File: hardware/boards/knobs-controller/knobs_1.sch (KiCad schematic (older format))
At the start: 28 parts, among them J1 ZX62-AB-5PA(31), J4 JST---S4B-PH-SM4-TB(LF)(SN)_J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, J8 2X3_SMD_MALE, U3 MK1_ZERO_ATSAMD21G18A-48, Y1 32.768KHz

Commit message: redo migrate from eagle
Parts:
- C11, C4, C6, C9: footprint KnobsController_v1.1:RESISTOR-NICK_C0805 -> knobs:RESISTOR-NICK_C0805; symbol KnobsController_v1.1-eagle-import:RESISTOR-NICK_C-EUC0805 -> knobs-eagle-import:RESISTOR-NICK_C-EUC0805
- C5: footprint KnobsController_v1.1:RESISTOR-NICK_C1206 -> knobs:RESISTOR-NICK_C1206; symbol KnobsController_v1.1-eagle-import:RESISTOR-NICK_C-EUC1206 -> knobs-eagle-import:RESISTOR-NICK_C-EUC1206
- C7: footprint KnobsController_v1.1:C0805 -> knobs:C0805; symbol KnobsController_v1.1-eagle-import:C-EUC0805 -> knobs-eagle-import:C-EUC0805
- D1: footprint KnobsController_v1.1:MK1_ZERO_SOT190P230X110-4N -> knobs:MK1_ZERO_SOT190P230X110-4N; symbol KnobsController_v1.1-eagle-import:MK1_ZERO_PRTR5V0U2X,215 -> knobs-eagle-import:MK1_ZERO_PRTR5V0U2X,215
- D2: footprint KnobsController_v1.1:LED_RADIAL_3MM -> knobs:LED_RADIAL_3MM; symbol KnobsController_v1.1-eagle-import:LED_LTL-1CHG -> knobs-eagle-import:LED_LTL-1CHG
- D3: footprint KnobsController_v1.1:MK1_ZERO_SODFL1008X40N-882D -> knobs:MK1_ZERO_SODFL1008X40N-882D; symbol KnobsController_v1.1-eagle-import:MK1_ZERO_PMEG2005EL -> knobs-eagle-import:MK1_ZERO_PMEG2005EL
- F2: footprint KnobsController_v1.1:MK1_ZERO_0603-F1608X100N -> knobs:MK1_ZERO_0603-F1608X100N; symbol KnobsController_v1.1-eagle-import:MK1_ZERO_MF-FSMF050X-2 -> knobs-eagle-import:MK1_ZERO_MF-FSMF050X-2
- J1: footprint KnobsController_v1.1:MK1_ZERO_USBMICRO-ZX62-AB-5PA -> knobs:MK1_ZERO_USBMICRO-ZX62-AB-5PA; symbol KnobsController_v1.1-eagle-import:MK1_ZERO_ZX62AB-5PA(11) -> knobs-eagle-import:MK1_ZERO_ZX62AB-5PA(11)
- J4: footprint KnobsController_v1.1:JST---S4B-PH-SM4-TB(LF)(SN)_JST_S4B-PH-SM4-TB_LF_SN_0 -> knobs:JST---S4B-PH-SM4-TB(LF)(SN)_JST_S4B-PH-SM4-TB_LF_SN_0; symbol KnobsController_v1.1-eagle-import:JST---S4B-PH-SM4-TB(LF)(SN)_JST_S4B-PH-SM4-TB_LF_SNJST_S4B-PH-SM4-TB_LF_SN_0_0 -> knobs-eagle-import:JST---S4B-PH-SM4-TB(LF)(SN)_JST_S4B-PH-SM4-TB_LF_SNJST_S4B-PH-SM4-TB_LF_SN_0_0
- J8: footprint KnobsController_v1.1:2X3_SMT -> knobs:2X3_SMT; symbol KnobsController_v1.1-eagle-import:2X3_SMD_MALE -> knobs-eagle-import:2X3_SMD_MALE
- L2: footprint KnobsController_v1.1:MK1_ZERO_0603-1608X90N -> knobs:MK1_ZERO_0603-1608X90N; symbol KnobsController_v1.1-eagle-import:MK1_ZERO_BLM18PG471SN1D -> knobs-eagle-import:MK1_ZERO_BLM18PG471SN1D
- R13, R15, R16, R20, R7: footprint KnobsController_v1.1:R0805 -> knobs:R0805; symbol KnobsController_v1.1-eagle-import:R-EU_R0805 -> knobs-eagle-import:R-EU_R0805
- R18, R2: footprint KnobsController_v1.1:RESISTOR-NICK_R0805 -> knobs:RESISTOR-NICK_R0805; symbol KnobsController_v1.1-eagle-import:RESISTOR-NICK_R-EU_R0805 -> knobs-eagle-import:RESISTOR-NICK_R-EU_R0805
- U$9: footprint KnobsController_v1.1:C&K_PTS820_NOPEGS -> knobs:C&K_PTS820_NOPEGS; symbol KnobsController_v1.1-eagle-import:PUSHBUTTON2 -> knobs-eagle-import:PUSHBUTTON2
- U3: footprint KnobsController_v1.1:MK1_ZERO_QFN50P700X700X90-49XN-EPSQ515 -> knobs:MK1_ZERO_QFN50P700X700X90-49XN-EPSQ515; symbol KnobsController_v1.1-eagle-import:MK1_ZERO_ATSAMD21G18A-48 -> knobs-eagle-import:MK1_ZERO_ATSAMD21G18A-48
- VR1, VR2, VR3, VR4: footprint KnobsController_v1.1:MUSICTHINGMODULAR_9MM_SNAP-IN_POT -> knobs:MUSICTHINGMODULAR_9MM_SNAP-IN_POT; symbol KnobsController_v1.1-eagle-import:MUSICTHINGMODULAR_9MM_SNAP-IN_POT_ -> knobs-eagle-import:MUSICTHINGMODULAR_9MM_SNAP-IN_POT_
- Y1: footprint KnobsController_v1.1:MK1_ZERO_QUARZO-ABS07 -> knobs:MK1_ZERO_QUARZO-ABS07; symbol KnobsController_v1.1-eagle-import:MK1_ZERO_ABS07-32.768KHZ-T -> knobs-eagle-import:MK1_ZERO_ABS07-32.768KHZ-T
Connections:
- net labels removed: +3.3V
- wire segments 176 -> 167

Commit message: cleanup
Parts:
- U3: value MK1_ZERO_ATSAMD21G18A-48 -> ATSAMD21G18A-48
- VR1, VR2, VR3, VR4: value MUSICTHINGMODULAR_9MM_SNAP-IN_POT_ -> 50k
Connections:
- net labels removed: MK1_ZERO_+3V3
- wire segments 167 -> 158
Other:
- note removed: "Arturo Guadalupi"
- note removed: "Crypto\nAuth"
- moved on the sheet: D2, R18, VR1, VR2, VR3, VR4

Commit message: minor cleanup
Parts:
- F2: value MK1_ZERO_MF-FSMF050X-2 -> MF-FSMF050X-2
- L2: value MK1_ZERO_BLM18PG471SN1D -> BLM18PG471SN1D
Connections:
- net labels removed: MK1_ZERO_VUSB
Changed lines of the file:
@@
 Wire Wire Line
 	3400 3400 4400 3400
-Text Label 3900 3400 0    70   ~ 0
+Text Label 3600 3400 0    70   ~ 0
 PA18_USB_ID
 Wire Wire Line
@@
 	2700 3100 2700 3300
 Connection ~ 2700 3300
-Text Label 3550 3300 0    70   ~ 0
+Text Label 3600 3300 0    70   ~ 0
 USB_P
 Wire Wire Line
@@
 	2600 2900 2600 3200
 Connection ~ 2600 3200
-Text Label 3500 3200 0    70   ~ 0
+Text Label 3600 3200 0    70   ~ 0
 USB_N
 Wire Wire Line
@@
 $EndComp
 $Comp
-L knobs-eagle-import:MK1_ZERO_BLM18PG471SN1D L2
-U 1 1 9F8286A9
-P 3400 2300
-AR Path="/9F8286A9" Ref="L2"  Part="1"
-AR Path="/5D86641C/9F8286A9" Ref="L2"  Part="1"
-F 0 "L2" H 3400 2460 59  0000 C BNN
-F 1 "MK1_ZERO_BLM18PG471SN1D" H 3400 2370 59  0000 C BNN
-F 2 "knobs:MK1_ZERO_0603-1608X90N" H 3400 2300 50  0001 C CNN
-F 3 "" H 3400 2300 50  0001 C CNN
-	1    3400 2300
-	1    0    0    -1
-$EndComp
-$Comp
 L knobs-eagle-import:MK1_ZERO_PRTR5V0U2X,215 D1
 U 1 1 DA5D11AB
@@
 $EndComp
 $Comp
-L knobs-eagle-import:MK1_ZERO_VUSB #U$2
-U 1 1 6197D135
-P 4100 2100
-AR Path="/6197D135" Ref="#U$2"  Part="1"
-AR Path="/5D86641C/6197D135" Ref="#U$02"  Part="1"
-F 0 "#U$02" H 4100 2100 50  0001 C CNN
-F 1 "MK1_ZERO_VUSB" H 4100 2120 59  0000 C BNN
-F 2 "" H 4100 2100 50  0001 C CNN
-F 3 "" H 4100 2100 50  0001 C CNN
-	1    4100 2100
-	1    0    0    -1
-$EndComp
-$Comp
 L knobs-eagle-import:SUPPLY1_GND #GND9
 U 1 1 158B4DC7
@@
 AR Path="/5D86641C/5B319BB3" Ref="F2"  Part="1"
 F 0 "F2" V 2579 2300 59  0000 C TNN
-F 1 "MK1_ZERO_MF-FSMF050X-2" V 2425 2300 59  0000 C BNN
+F 1 "MF-FSMF050X-2" V 2425 2300 59  0000 C BNN
 F 2 "knobs:MK1_ZERO_0603-F1608X100N" H 2500 2300 50  0001 C CNN
 F 3 "" H 2500 2300 50  0001 C CNN
@@
 Wire Bus Line
 	7800 7200 7800 9600
+$Comp
+L knobs-eagle-import:MK1_ZERO_BLM18PG471SN1D L2
+U 1 1 9F8286A9
+P 3400 2300
+AR Path="/9F8286A9" Ref="L2"  Part="1"
+AR Path="/5D86641C/9F8286A9" Ref="L2"  Part="1"
+F 0 "L2" H 3400 2460 59  0000 C BNN
+F 1 "BLM18PG471SN1D" H 3400 2370 59  0000 C BNN
+F 2 "knobs:MK1_ZERO_0603-1608X90N" H 3400 2300 50  0001 C CNN
+F 3 "" H 3400 2300 50  0001 C CNN
+	1    3400 2300
+	1    0    0    -1
+$EndComp
+$Comp
+L knobs-eagle-import:+3V3 #+3V?
+U 1 1 5D890552
+P 4100 2100
+AR Path="/5D890552" Ref="#+3V?"  Part="1"
+AR Path="/5D86641C/5D890552" Ref="#+3V?"  Part="1"
+F 0 "#+3V?" H 4100 2100 50  0001 C CNN
+F 1 "+3V3" H 4100 2120 59  0000 C BNN
+F 2 "" H 4100 2100 50  0001 C CNN
+F 3 "" H 4100 2100 50  0001 C CNN
+	1    4100 2100
+	1    0    0    -1
+$EndComp
 $EndSCHEMATC

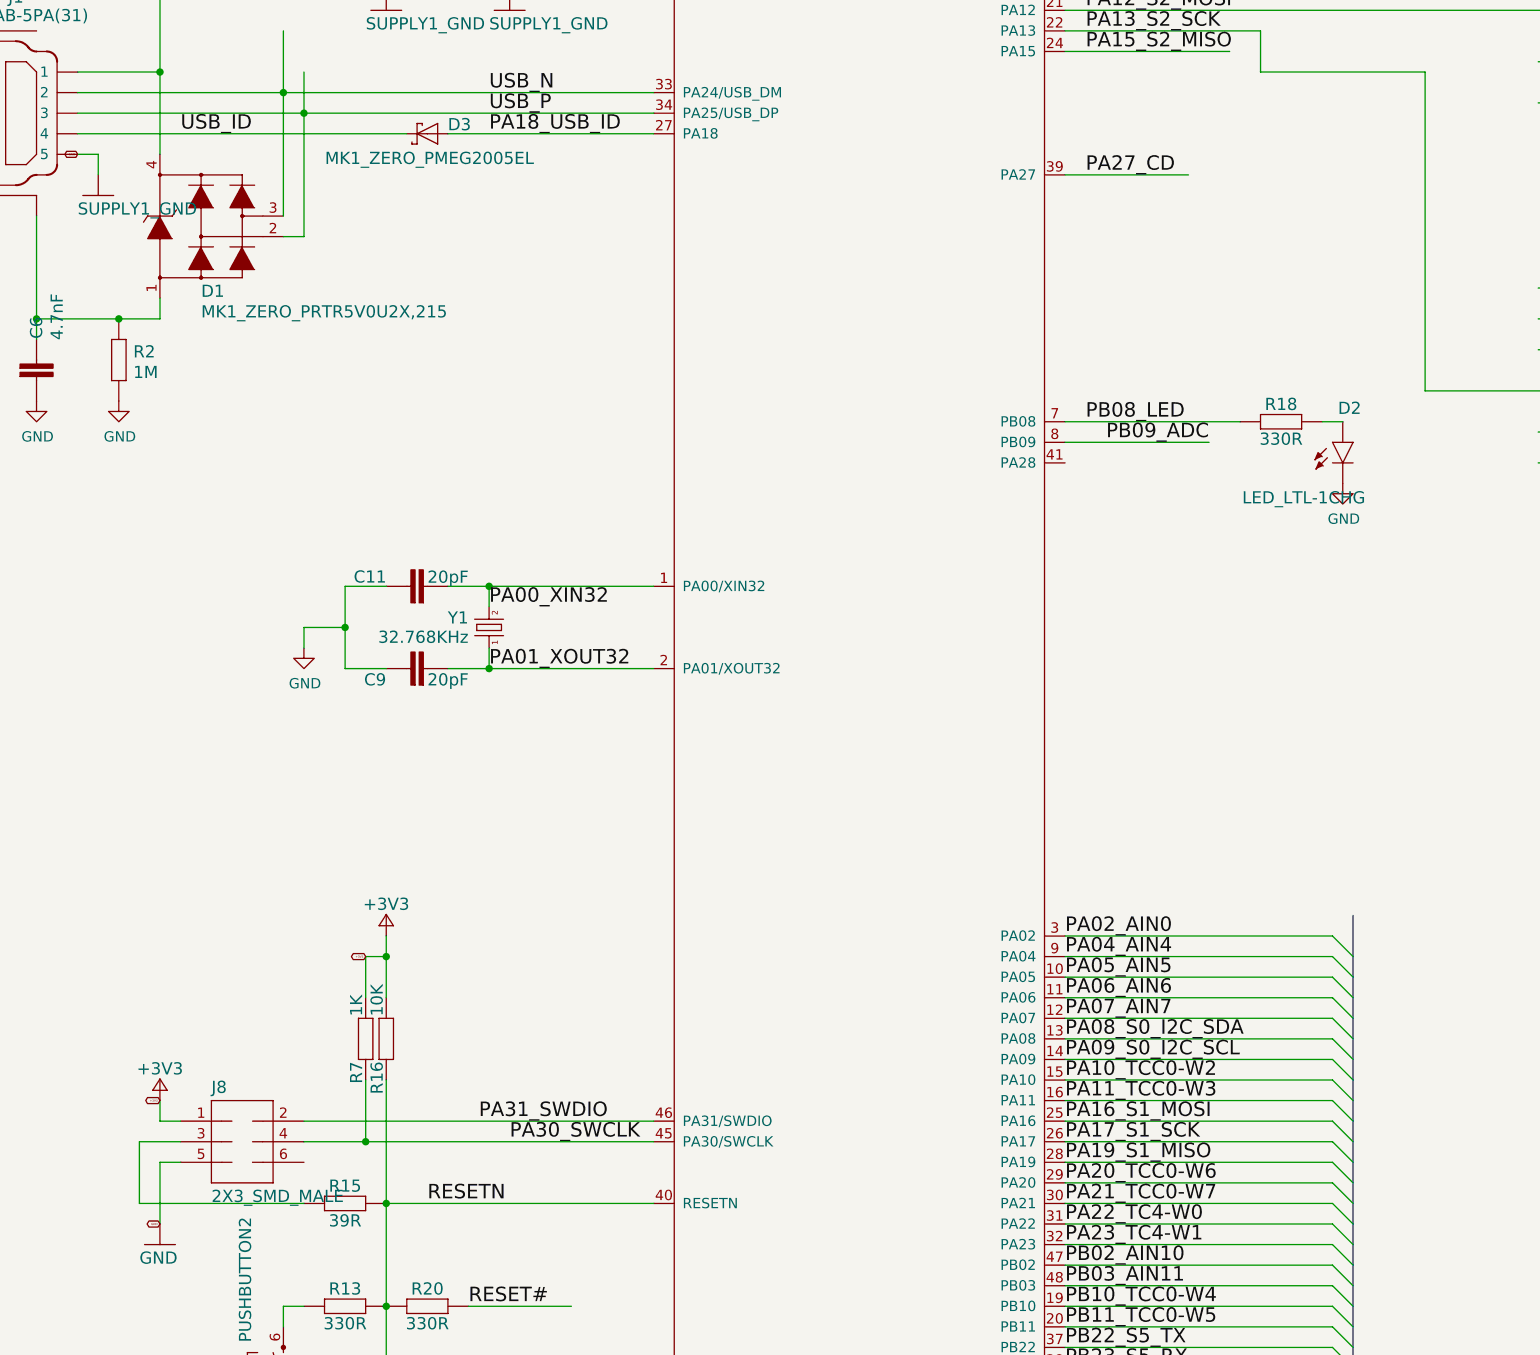
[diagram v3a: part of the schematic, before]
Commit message: silkscreen improvement
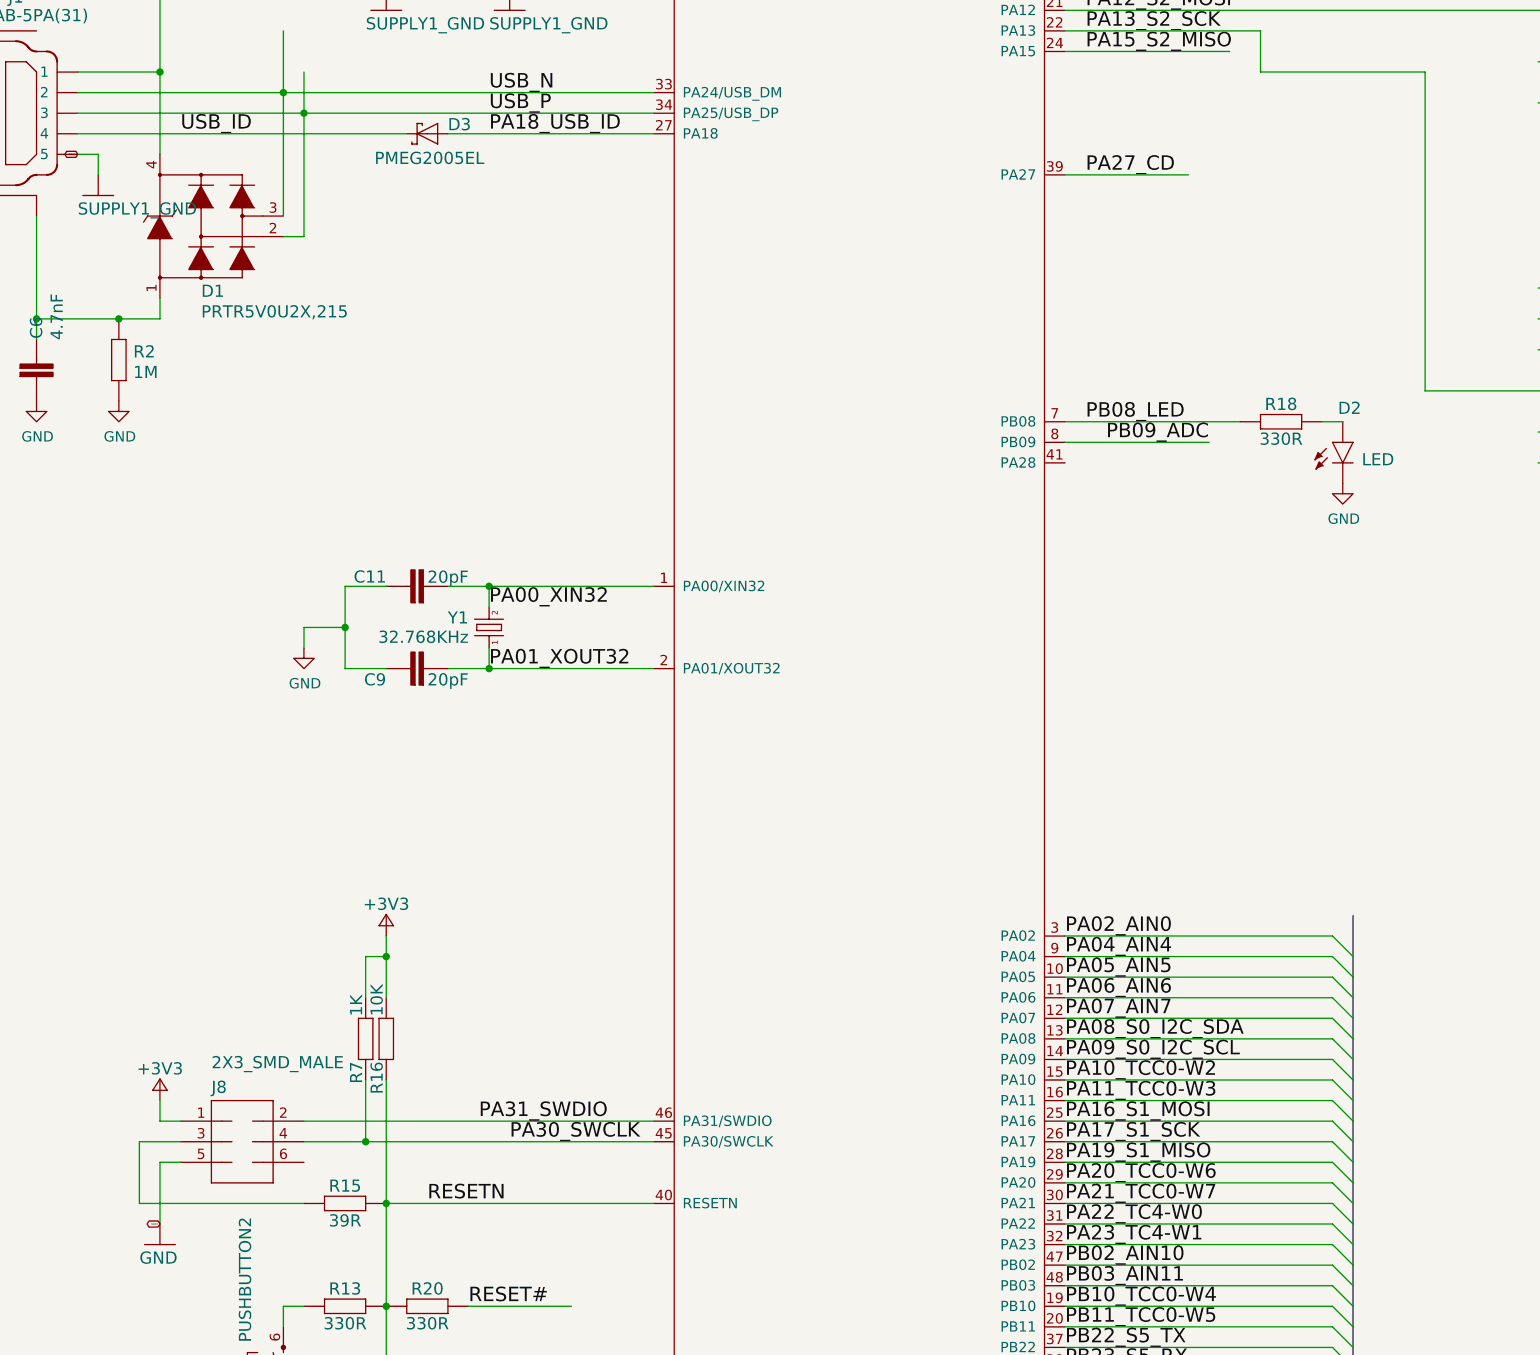
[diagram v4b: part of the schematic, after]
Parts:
- D1: value MK1_ZERO_PRTR5V0U2X,215 -> PRTR5V0U2X,215
- D2: value LED_LTL-1CHG -> LED
- D3: value MK1_ZERO_PMEG2005EL -> PMEG2005EL
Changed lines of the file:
@@
 Wire Wire Line
 	2000 8200 2100 8200
-Text GLabel 2000 8100 0    10   BiDi ~ 0
-+3V3
 Wire Wire Line
 	3000 7400 3000 7600
@@
 	3100 7400 3100 7300
 Connection ~ 3100 7400
-Text GLabel 3000 7400 0    10   BiDi ~ 0
-+3V3
 Wire Wire Line
 	3400 3400 4400 3400
@@
 AR Path="/5D86641C/DA5D11AB" Ref="D1"  Part="1"
 F 0 "D1" H 2200 3400 59  0000 L BNN
-F 1 "MK1_ZERO_PRTR5V0U2X,215" H 2200 3300 59  0000 L BNN
+F 1 "PRTR5V0U2X,215" H 2200 3300 59  0000 L BNN
 F 2 "knobs:MK1_ZERO_SOT190P230X110-4N" H 2200 3800 50  0001 C CNN
 F 3 "" H 2200 3800 50  0001 C CNN
@@
 AR Path="/5D86641C/16D8F47B" Ref="D3"  Part="1"
 F 0 "D3" H 3201 3390 59  0000 R TNN
-F 1 "MK1_ZERO_PMEG2005EL" H 3290 3485 59  0000 C BNN
+F 1 "PMEG2005EL" H 3290 3485 59  0000 C BNN
 F 2 "knobs:MK1_ZERO_SODFL1008X40N-882D" H 3300 3400 50  0001 C CNN
 F 3 "" H 3300 3400 50  0001 C CNN
@@
 AR Path="/5D86641C/74A9BC2C" Ref="D2"  Part="1"
 F 0 "D2" H 7840 5100 59  0000 R TNN
-F 1 "LED_LTL-1CHG" H 7860 4665 59  0000 R TNN
+F 1 "LED" H 8000 4850 59  0000 R TNN
 F 2 "knobs:LED_RADIAL_3MM" H 7750 4900 50  0001 C CNN
 F 3 "" H 7750 4900 50  0001 C CNN
@@
 AR Path="/5D86641C/C956E274" Ref="J8"  Part="1"
 F 0 "J8" H 2250 8530 59  0000 L BNN
-F 1 "2X3_SMD_MALE" H 2250 8000 59  0000 L BNN
+F 1 "2X3_SMD_MALE" H 2250 8650 59  0000 L BNN
 F 2 "knobs:2X3_SMT" H 2400 8300 50  0001 C CNN
 F 3 "" H 2400 8300 50  0001 C CNN
